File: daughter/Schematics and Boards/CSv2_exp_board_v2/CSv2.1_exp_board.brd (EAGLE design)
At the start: 51.4 x 47 mm, 103 parts, among them J1 HIROSE-DF40_50-PIN_CONNECTORS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, J3 CORTEX_DEBUG_SMD, J4 SJ-43514-SMTC, J6 ATTINY_AVR_DEBUG, J7 J-USB-HIROSE-MICRO-USB, SW1 SPST_TACT-KMR2, SW2 SPST_TACT-KMR2, U1 LOADSWITCH-MIC94164, U10 LOADSWITCH-MIC94164, U11 BMI160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

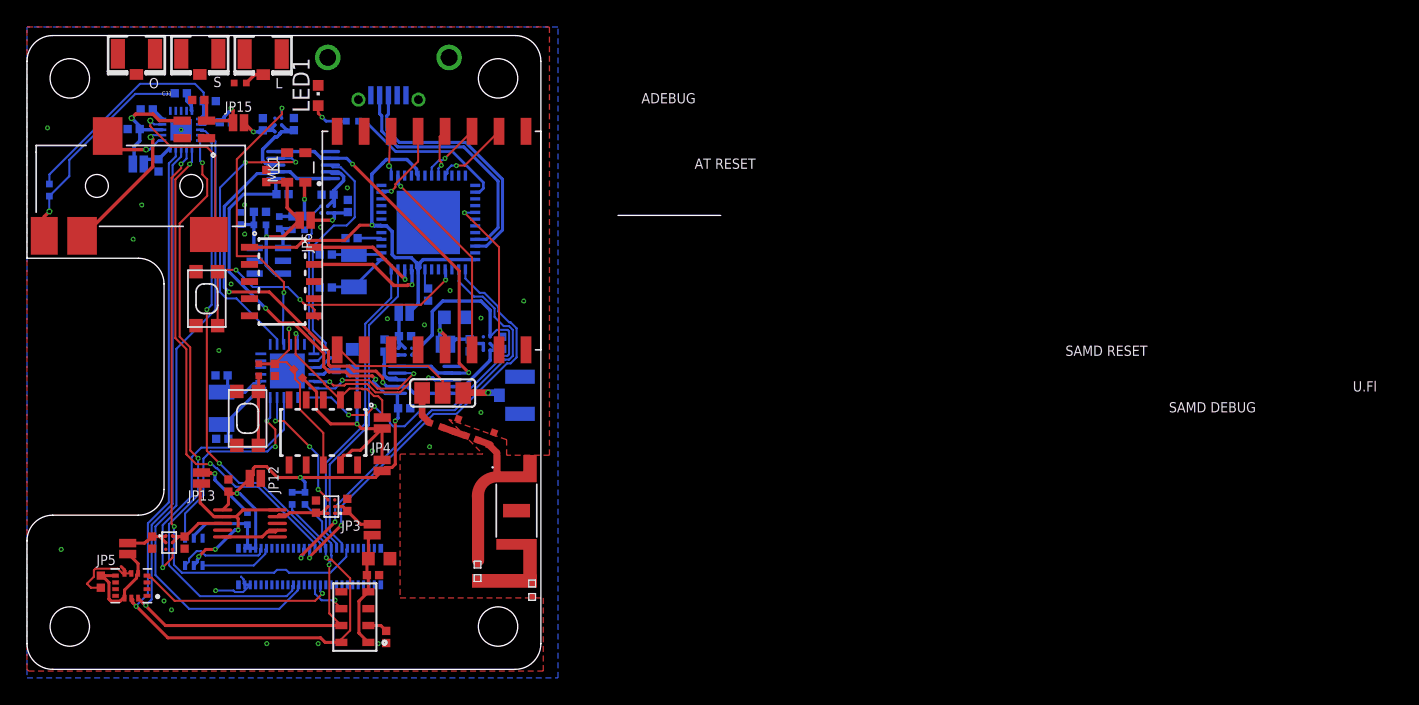
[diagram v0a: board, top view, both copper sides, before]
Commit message: DTRv2.1 finished routing
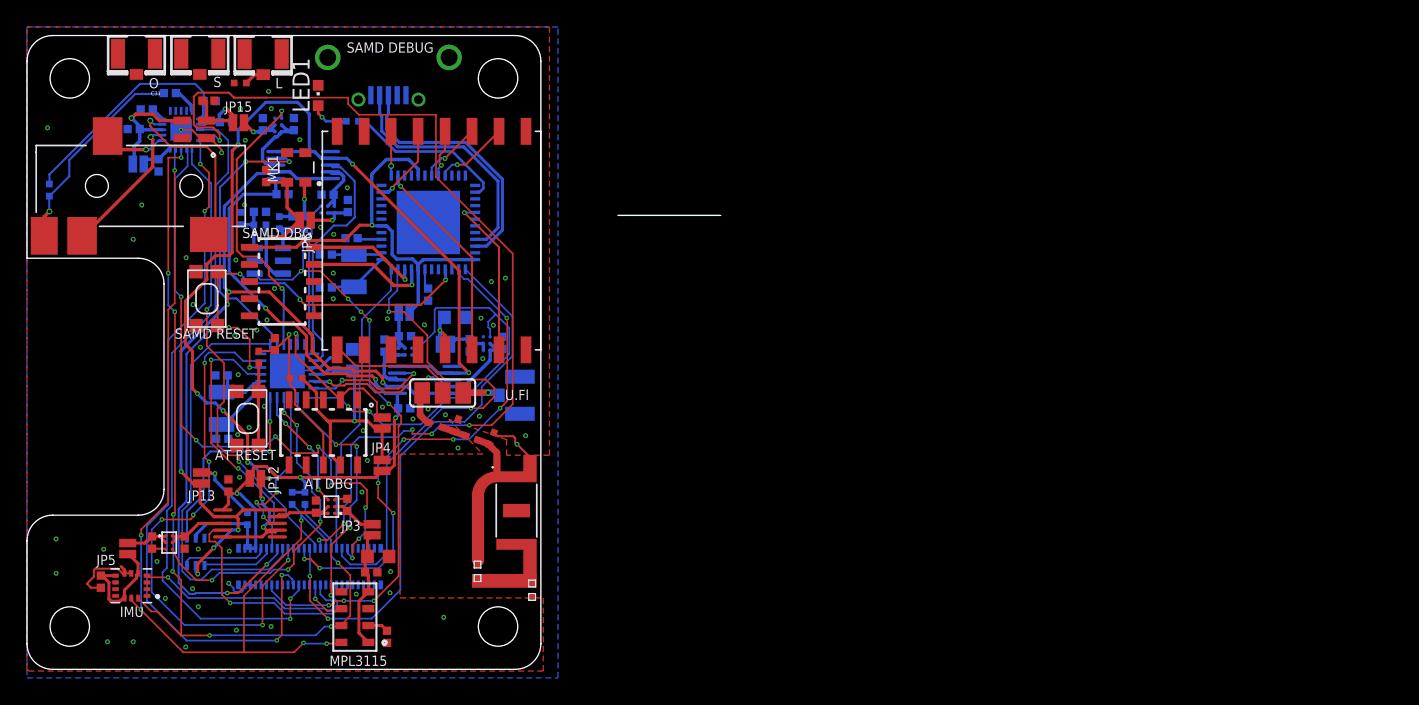
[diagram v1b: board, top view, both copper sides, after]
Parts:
- moved C46 1.91 mm to (18.4, 24.1), turned to 270 degrees
- moved R9 0.94 mm to (17.2, 23.2)
- moved C31 0.81 mm to (10.6, 42.7)
- moved C42 0.75 mm to (13.4, 42.2), turned to 0 degrees
- moved R10 0.38 mm to (20.0, 21.6), turned to 0 degrees
- moved C47 0.24 mm to (25.5, 7.19)
- moved C40 0.18 mm to (26.0, 8.37)
- moved U13 0.14 mm to (12.5, 8.71)
- moved C48 0.06 mm to (26.7, 2.41)
- turned C15 to 0 degrees
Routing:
- net +3V3_NMEAS: track 34.9 -> 80.5 mm, vias 2 -> 9
- net DTR_BUS1_GPIO2/AIN0: track 0.00 -> 44.9 mm, vias 0 -> 8
- net DTR_IRQ: track 0.00 -> 40.9 mm, vias 0 -> 6
- net DTR_BUS0_P2/I2S_FS0: track 35.7 -> 72.0 mm, vias 2 -> 6
- net MASTER_I2C_SCL: track 0.00 -> 35.3 mm, vias 0 -> 4
- net MEAS_IMU: track 0.00 -> 35.0 mm, vias 0 -> 5
- net DTR_DETECT: track 0.00 -> 31.1 mm
- net MASTER_I2C_SDA: track 0.00 -> 20.2 mm, vias 0 -> 2
- net +3V3_MEAS: track 49.6 -> 67.3 mm, vias 5 -> 7
- net DTR_BUS1_P0: track 23.2 -> 36.6 mm, vias 0 -> 2
- net GND: track 25.5 -> 38.7 mm, vias 24 -> 66
- net MEAS_BARO: track 0.00 -> 12.0 mm, vias 0 -> 3
- net DTR_BUS1_P2: track 31.5 -> 42.0 mm
- net DTR_BUS0_GPIO0/I2S_SCK: track 46.3 -> 53.5 mm, vias 2 -> 4
- net DTR_BUS1_P3: track 32.2 -> 38.1 mm, vias 2 -> 8
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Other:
- board text added: "AT DBG"
- board text added: "SAMD DBG"
- board text removed: "ADEBUG"

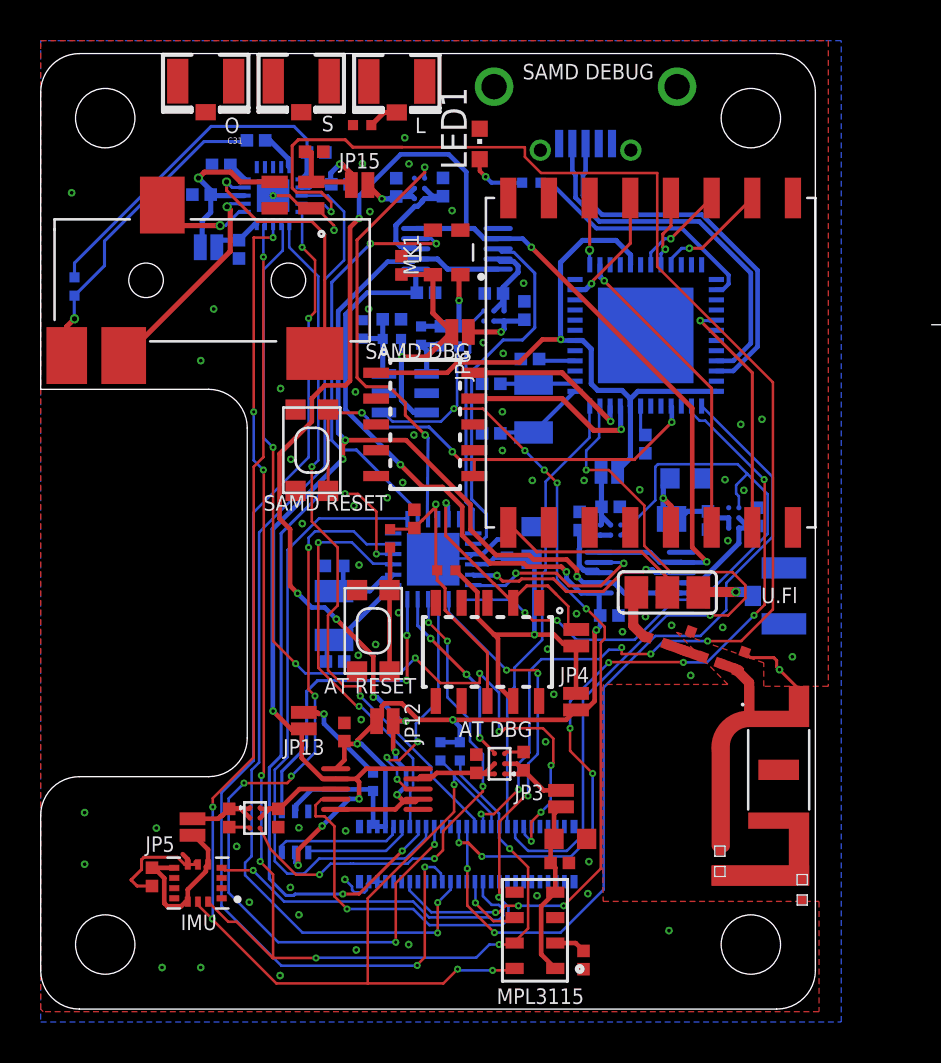
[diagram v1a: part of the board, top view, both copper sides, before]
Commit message: DTR: increase hole sizes
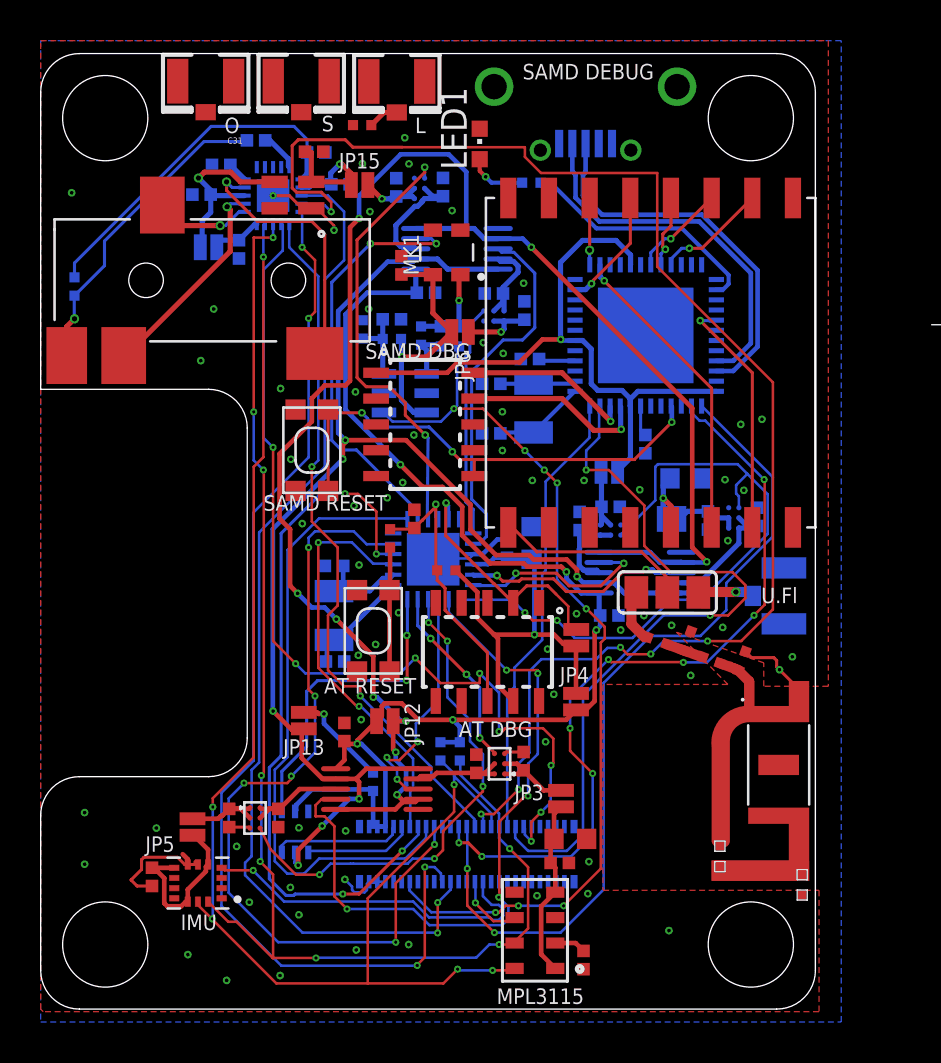
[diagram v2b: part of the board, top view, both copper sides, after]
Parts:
- moved A1 0.24 mm to (36.3, 12.0)
- moved C3 0.24 mm to (37.5, 6.10)
- moved C5 0.24 mm to (33.4, 7.50)

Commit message: File mgmt for manufacture prep. Minor change to DTR board + gen gerbers
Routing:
- removed copper zone on layer 2, net GND
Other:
- board size 51.4 x 47 mm -> 38.1 x 47 mm
